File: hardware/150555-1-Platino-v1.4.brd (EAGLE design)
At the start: 144.7 x 68.6 mm, 88 parts, among them IC1 MEGA164P/324P/644P-PU, IC2 MEGA48/88/168-PU, IC3 7805TV, IC4 MCP1700-3302, K1 EXT1, K10 K-HEADER-MALE-1X5-V, K11 K-HEADER-MALE-1X5-V, K12 K-TERMINAL-BLOCK-1X2-350, K2 K-HEADER-MALE-1X6-H, K3 K-HEADER-MALE-2X3-V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

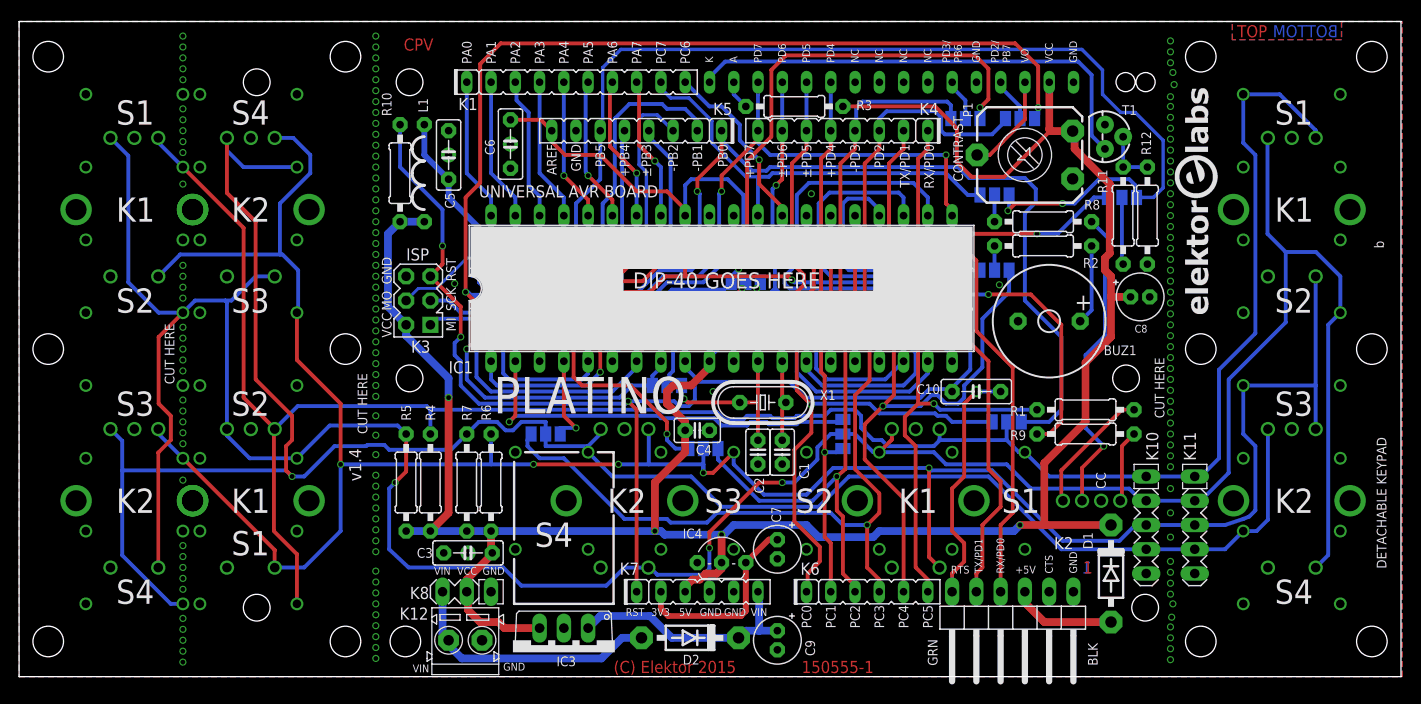
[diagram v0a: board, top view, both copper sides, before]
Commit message: Release
Fixed all OAR and hole-in-hole issues.
Minor silkscreen edits.
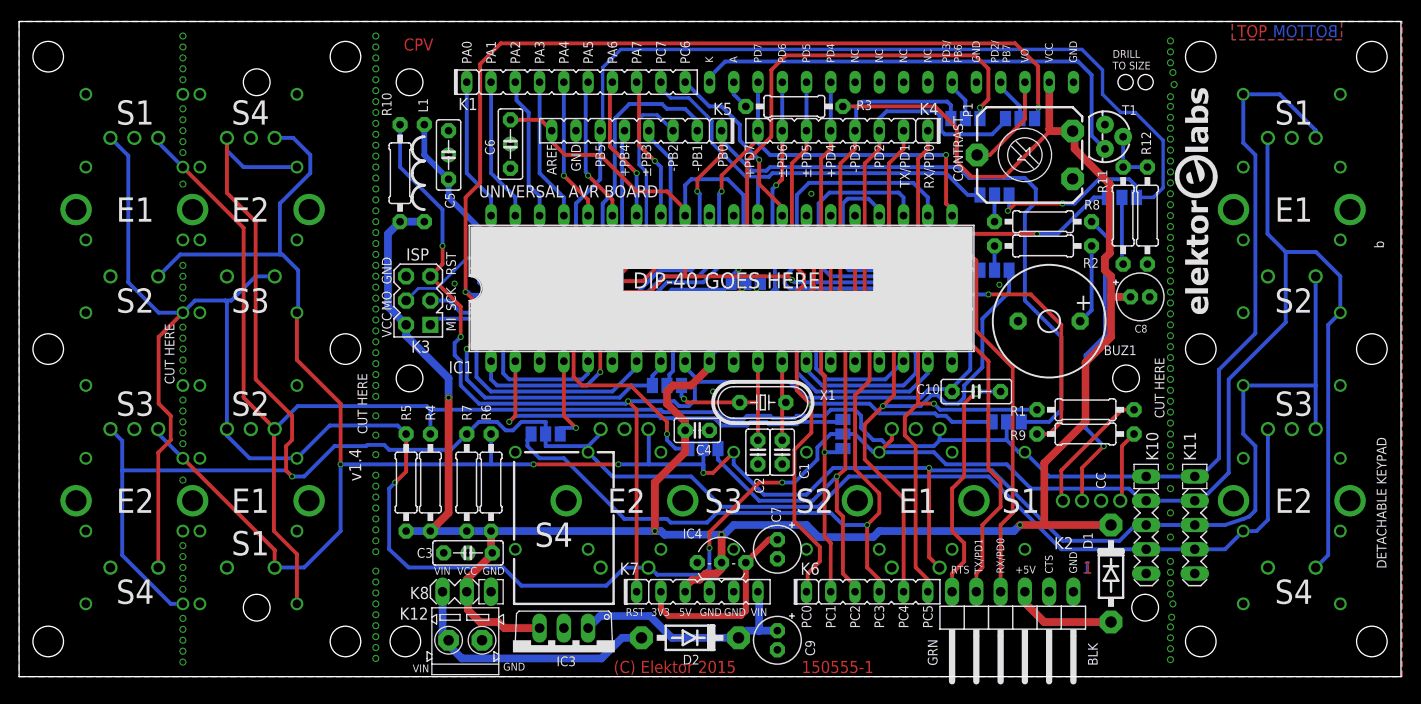
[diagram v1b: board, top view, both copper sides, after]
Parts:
- S5B, S6B: value EC12E_SW -> EC12E_SW_ALT1-B; device 000_cpv:ALPS_EC12E_SW -> 150555-1-Platino-v1.4:ALPS_EC12E_SW_ALT2
- moved U$2 1.33 mm to (43.9, 19.3)
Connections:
- net GND: no longer S5B.GND1, S6B.GND1
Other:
- board text added: "DRILL TO SIZE"
- board text added: "E1"
- board text added: "E2"
- board text removed: "CONFIGURE SOLDER JUMPERS!"
- board text removed: "K1"
- board text removed: "K2"
- board text removed: "LCD, LED1, IC2 (DIP-28), S1-S6 GO ON THIS SIDE"
- board text removed: "PLATINO"
